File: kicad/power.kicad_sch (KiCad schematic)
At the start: 12 parts, among them J1 Bus_PCI_Express_x1, J2 Conn_01x02_Pin, J6 USB_C_Receptacle_USB2.0_16P

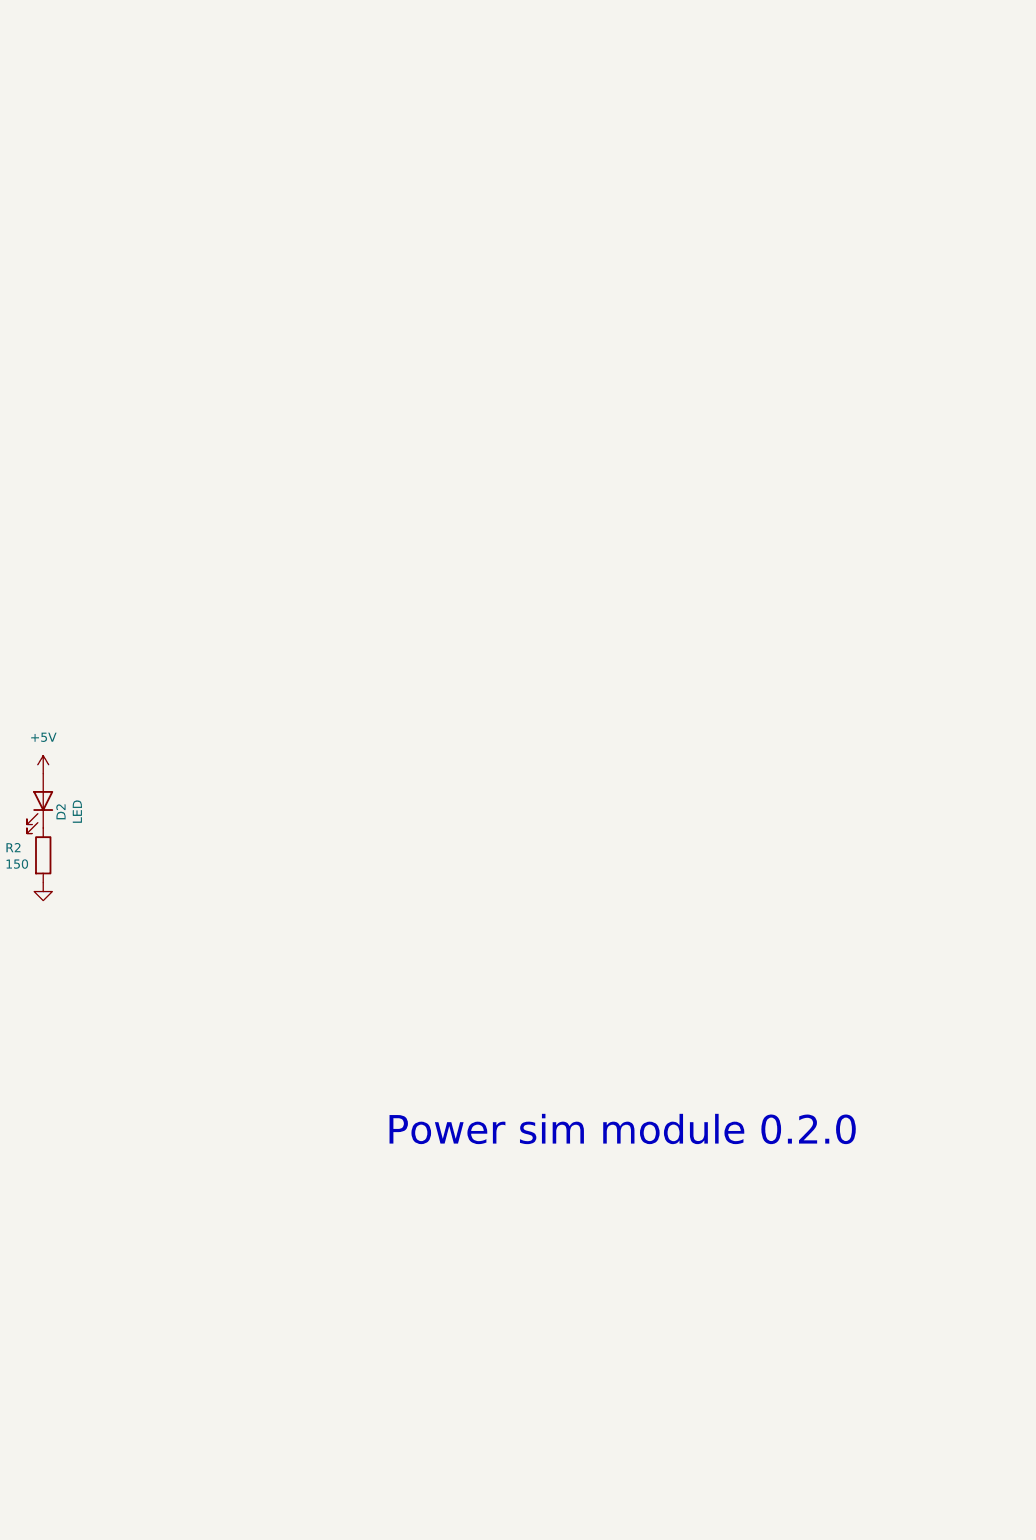
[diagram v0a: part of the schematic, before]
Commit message: feat: Add components for battery management, charging, and protection
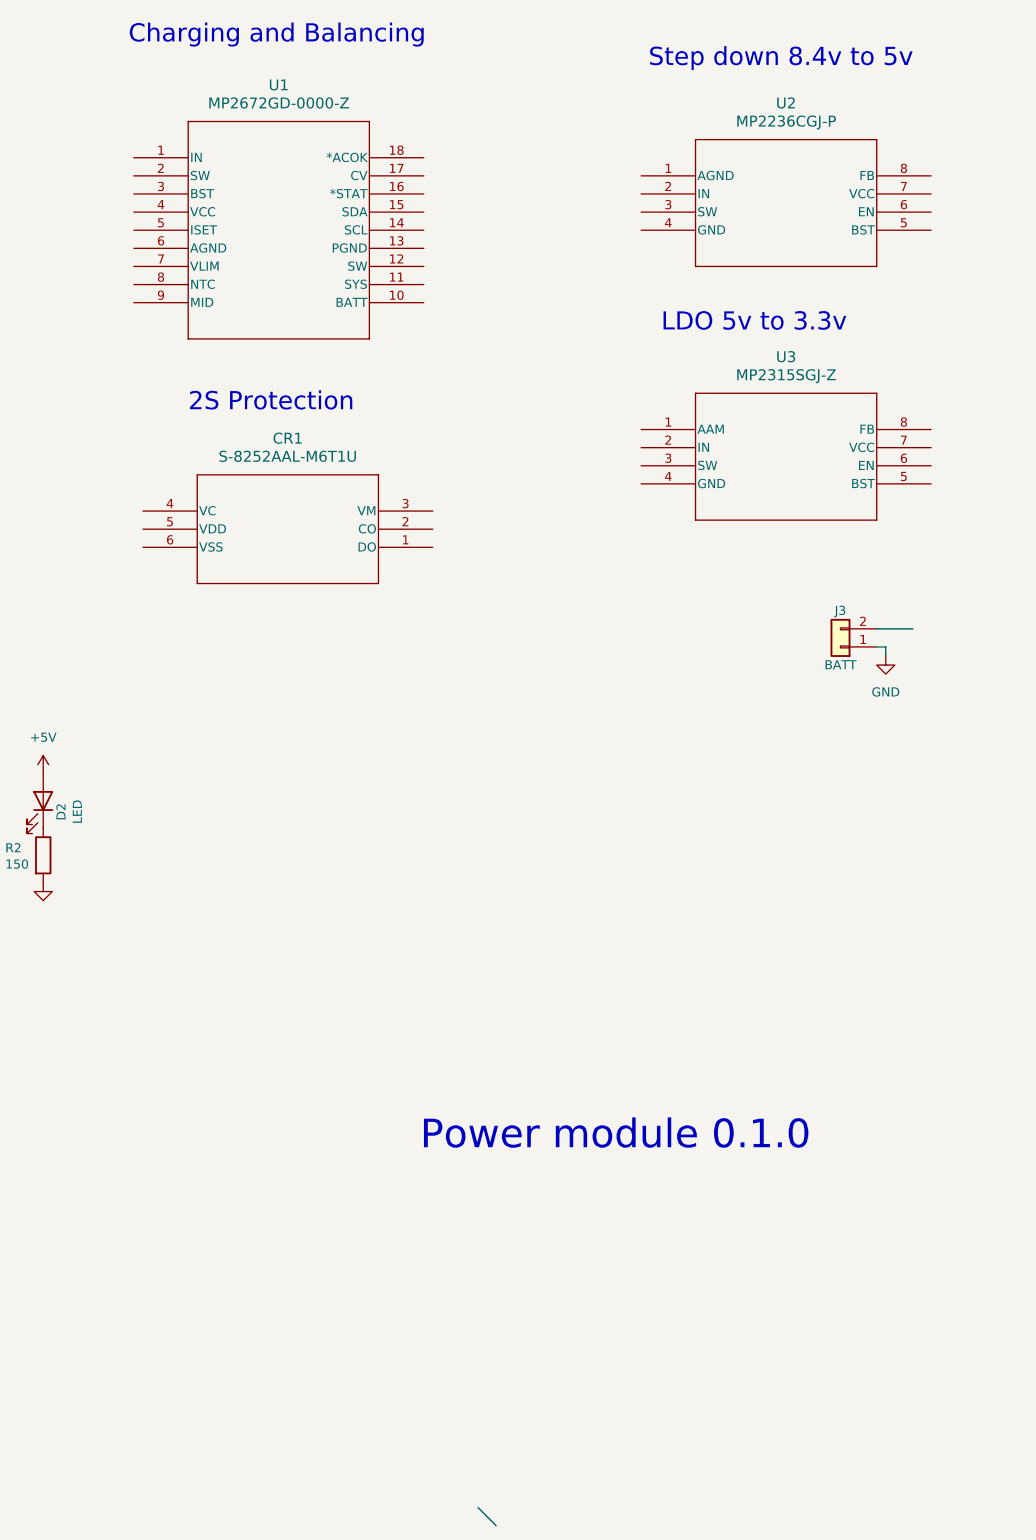
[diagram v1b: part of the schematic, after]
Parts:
- added CR1: S-8252AAL-M6T1U, SOT23-6L_STM, symbol powermodule:S-8252AAL-M6T1U
- added J3: BATT, Connector_AMASS:AMASS_XT30U-F_1x02_P5.0mm_Vertical, symbol Connector_Generic:Conn_01x02
- added U1: MP2672GD-0000-Z, POWERLIB:QFN-18_2MMx3MM_MP2672_MNP_MPS, symbol powermodule:MP2672GD-0000-Z
- added U2: MP2236CGJ-P, POWERLIB:TSOT23-8_MP2236C_MNP, symbol powermodule:MP2236CGJ-P
- added U3: MP2315SGJ-Z, TSOT23-8_MP2315S_MNP, symbol powermodule:MP2315SGJ-Z
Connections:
- net GND: now also J3.1 (Pin_1)
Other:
- note added: "2S Protection"
- note added: "Charging and Balancing"
- note added: "LDO 5v to 3.3v"
- note added: "Power module 0.1.0"
- note added: "Step down 8.4v to 5v"
- note removed: "Power sim module 0.2.0"

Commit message: feat: Update 2S protection
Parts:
- added C1, C2: 0.1u, Capacitor_SMD:C_0402_1005Metric, symbol Device:C
- added Q1, Q2: AO3400A, SOT-23-3_L2.9-W1.3-P1.90-LS2.4-BR, symbol powermodule:AO3400
- added R5: 2k, Resistor_SMD:R_0402_1005Metric, symbol Device:R
- added R6, R7: 470R, Resistor_SMD:R_0402_1005Metric, symbol Device:R
- R1, R2: value 150 -> 1k; footprint Resistor_SMD:R_0603_1608Metric -> Resistor_SMD:R_0402_1005Metric; JLC Link https://jlcpcb.com/partdetail/23535-0603WAF1500T5E/C22808 -> https://jlcpcb.com/partdetail/12256-0402WGF1001TCE/C11702; LCSC Part # C22808 -> C11702; info 150 ohm -> 1k ohm; price C$0.0013 -> C$0.0007
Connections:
- net at CR1.1 (DO): now also Q2.1 (G)
- net at CR1.2 (CO): now also Q1.3 (D), Q2.3 (D)
- net at CR1.3 (VM): now also R5.2
- net at CR1.4 (VC): now also C2.2, R7.2
- net at CR1.5 (VDD): now also C1.1, R6.2
- net B_GND: now reaches CR1.6 (VSS)
- net B_GND: now also C1.2, C2.1, Q2.2 (S)
- new net +4.2V: R7.1
- new net +8.4V: R6.1
- new net LOAD_GND: Q1.2 (S), R5.1
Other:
- moved on the sheet: CR1

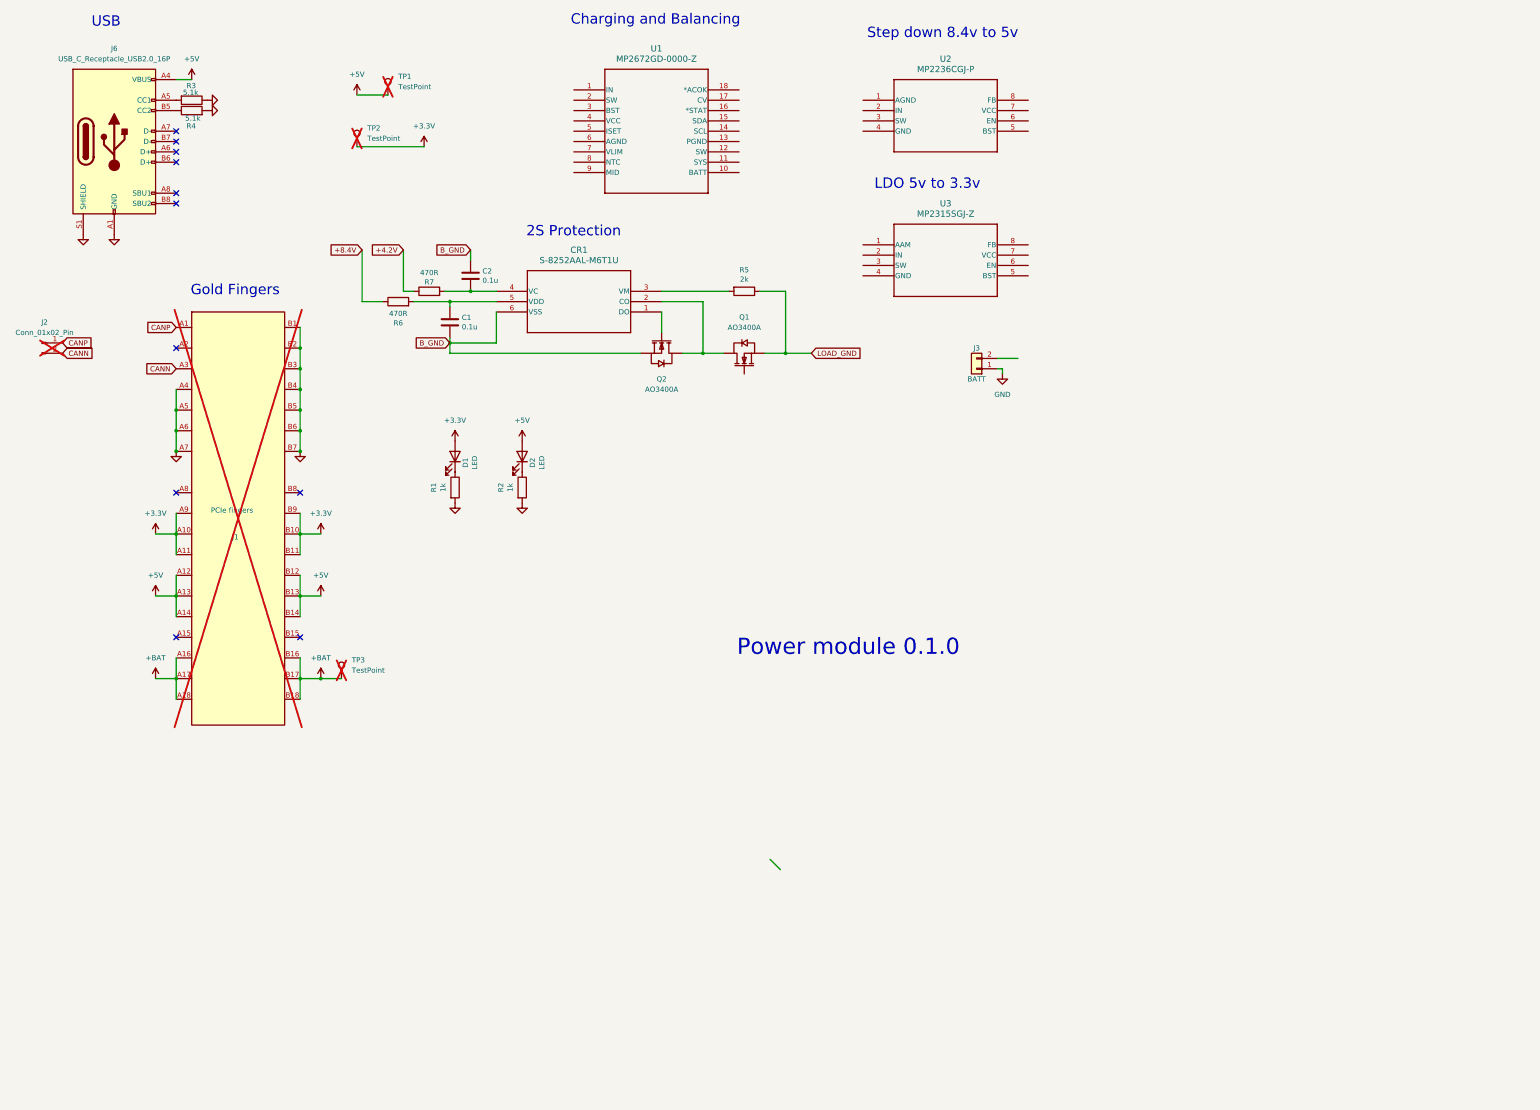
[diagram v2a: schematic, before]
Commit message: feat: Update 8.4V to 5V DC-DC converter
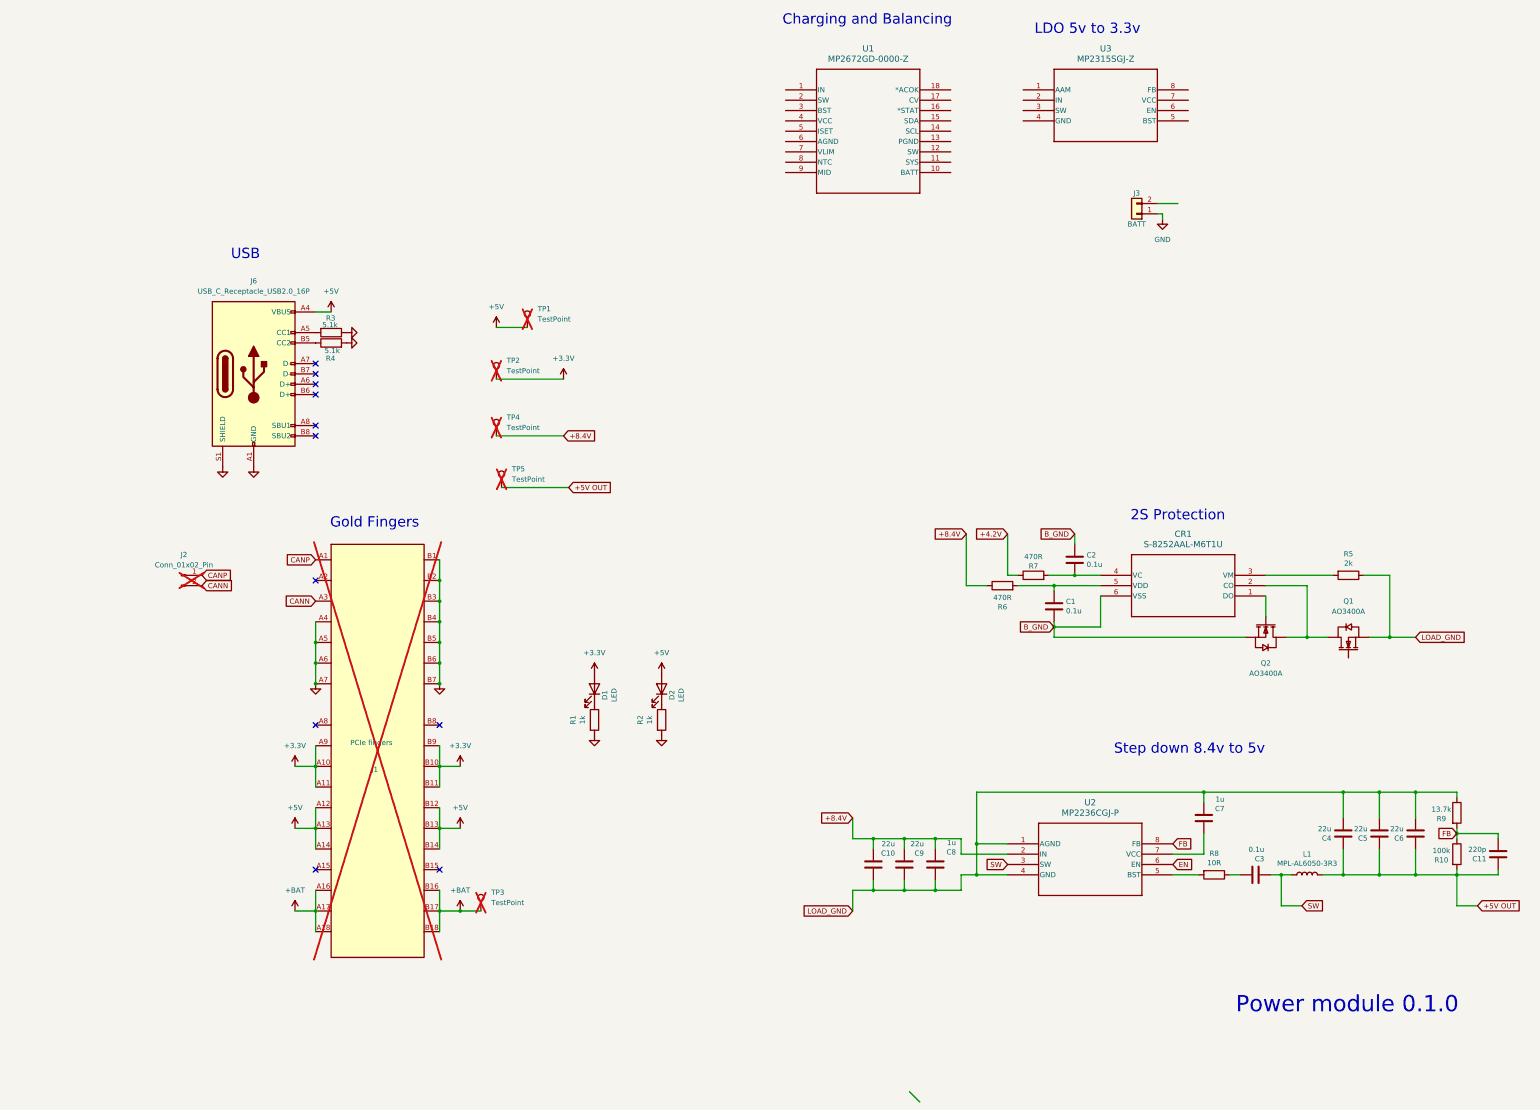
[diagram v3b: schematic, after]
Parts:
- added C10, C4, C5, C6, C9: 22u, Capacitor_SMD:C_0402_1005Metric, symbol Device:C
- added C11: 220p, Capacitor_SMD:C_0402_1005Metric, symbol Device:C
- added C3: 0.1u, Capacitor_SMD:C_0402_1005Metric, symbol Device:C
- added C7, C8: 1u, Capacitor_SMD:C_0402_1005Metric, symbol Device:C
- added L1: MPL-AL6050-3R3, POWERLIB:2-SMD, symbol Device:L
- added R10: 100k, Resistor_SMD:R_0402_1005Metric, symbol Device:R
- added R8: 10R, Resistor_SMD:R_0402_1005Metric, symbol Device:R
- added R9: 13.7k, Resistor_SMD:R_0402_1005Metric, symbol Device:R
- added TP4, TP5: TestPoint, Connector_PinHeader_2.54mm:PinHeader_1x01_P2.54mm_Vertical, symbol Connector:TestPoint
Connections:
- net +8.4V: now also U2.2 (IN), C10.2, C8.1, C9.2, TP4.1
- net LOAD_GND: now also U2.1 (AGND), U2.4 (GND), C10.1, C4.2, C5.2, C6.2, C7.1, C8.2, C9.1, R9.1
- net SW: now reaches U2.3 (SW)
- net SW: now also C3.2, L1.1
- net at U2.5 (BST): now also R8.2
- net EN: now reaches U2.6 (EN)
- net at U2.7 (VCC): now also C7.2
- net FB: now reaches U2.8 (FB)
- net FB: now also C11.2, R10.1, R9.2
- new net: C3.1, R8.1
- new net +5V OUT: C11.1, C4.1, C5.1, C6.1, L1.2, R10.2, TP5.1
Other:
- moved on the sheet: C1, C2, CR1, D1, D2, J1, J2, J3, J6, Q1, Q2, R1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

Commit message: feat: Update 8.4V to 3.3V DC-DC converter
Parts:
- removed U3: MP2315SGJ-Z, TSOT23-8_MP2315S_MNP, symbol powermodule:MP2315SGJ-Z
- added C12, C13, C17, C18, C19: 22u, Capacitor_SMD:C_0402_1005Metric, symbol Device:C
- added C14, C15: 1u, Capacitor_SMD:C_0402_1005Metric, symbol Device:C
- added C16: 0.1u, Capacitor_SMD:C_0402_1005Metric, symbol Device:C
- added C20: 220p, Capacitor_SMD:C_0402_1005Metric, symbol Device:C
- added L2: MPL-AL6050-2R2, POWERLIB:2-SMD, symbol Device:L
- added R11: 10R, Resistor_SMD:R_0402_1005Metric, symbol Device:R
- added R12: 22.1k, Resistor_SMD:R_0402_1005Metric, symbol Device:R
- added R13: 100k, Resistor_SMD:R_0402_1005Metric, symbol Device:R
- added U3: MP2236CGJ-P, POWERLIB:TSOT23-8_MP2236C_MNP, symbol powermodule:MP2236CGJ-P
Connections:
- net EN is gone; now on net +8.4V: U2.6 (EN)
- net +8.4V: now also C12.2, C13.2, C14.1, U3.2 (IN), U3.6 (EN)
- net LOAD_GND: now also C12.1, C13.1, C14.2, C15.1, C17.2, C18.2, C19.2, R12.1, U3.1 (AGND), U3.4 (GND)
- net FB renamed FB1
- net SW renamed SW1
- new net: C15.2, U3.7 (VCC)
- new net: C16.1, R11.1
- new net: R11.2, U3.5 (BST)
- new net +3.3V OUT: C17.1, C18.1, C19.1, C20.1, L2.2, R13.2
- new net FB2: C20.2, R12.2, R13.1, U3.8 (FB)
- new net SW2: C16.2, L2.1, U3.3 (SW)
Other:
- moved on the sheet: C1, C10, C11, C2, C3, C4, C5, C6, C7, C8, C9, CR1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

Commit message: feat: add charging
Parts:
- removed J3: BATT, Connector_AMASS:AMASS_XT30U-F_1x02_P5.0mm_Vertical, symbol Connector_Generic:Conn_01x02
- removed TP1: TestPoint, Connector_PinHeader_2.54mm:PinHeader_1x01_P2.54mm_Vertical, symbol Connector:TestPoint
- added C21, C24: 10u, Capacitor_SMD:C_0402_1005Metric, symbol Device:C
- added C22, C25: 22u, Capacitor_SMD:C_0402_1005Metric, symbol Device:C
- added C23: 1u, Capacitor_SMD:C_0402_1005Metric, symbol Device:C
- added C26: 100n, Capacitor_SMD:C_0402_1005Metric, symbol Device:C
- added D3, D4: LED, symbol Device:LED
- added L3: 1.5uH, IND-SMD_L7.0-W6.6, symbol powermodule:MWSA0605S-1R5MT
- added R14: 5.5k, Resistor_SMD:R_0402_1005Metric, symbol Device:R
- added R15, R24: 100R, Resistor_SMD:R_0402_1005Metric, symbol Device:R
- added R16: 30k, Resistor_SMD:R_0402_1005Metric, symbol Device:R
- added R17, R23: 60R, Resistor_SMD:R_0402_1005Metric, symbol Device:R
- added R18: 8k, Resistor_SMD:R_0402_1005Metric, symbol Device:R
- added R19: 12.6k, Resistor_SMD:R_0402_1005Metric, symbol Device:R
- added R20: 3.6k, Resistor_SMD:R_0402_1005Metric, symbol Device:R
- added R21: 2k, Resistor_SMD:R_0402_1005Metric, symbol Device:R
- added R22: NTCG103JF103FT1, POWERLIB:NTC_R0402, symbol powermodule:NTCG103JF103FT1
- added TP6: TestPoint, Connector_PinHeader_2.54mm:PinHeader_1x01_P2.54mm_Vertical, symbol Connector:TestPoint
- added U4: MR30-M, POWERLIB:CONN-TH_MR30-M, symbol powermodule:MR30
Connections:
- net +3.3V: no longer TP2.1
- net +3.3V OUT: now also TP2.1
- net +4.2V: now also R17.2, R23.2, TP6.1, U4.2
- net +5V: no longer J6.A4 (VBUS), J6.A9 (VBUS), J6.B4 (VBUS), J6.B9 (VBUS)
- net +8.4V: now also U1.10 (BATT), C25.1, U4.1
- net B_GND: now also U4.3
- net GND: no longer J6.A1 (GND), J6.A12 (GND), J6.B1 (GND), J6.B12 (GND), J6.S1 (SHIELD), R3.1, R4.2
- net LOAD_GND: now also J6.A1 (GND), J6.A12 (GND), J6.B1 (GND), J6.B12 (GND), J6.S1 (SHIELD), R3.1, R4.2, U1.13 (PGND), U1.6 (AGND), C21.2, C22.1, C23.2, C24.2, C25.2, R16.2, R18.2, R21.1, R22.1
- net VIN: now reaches U1.1 (IN)
- net VIN: now also J6.A4 (VBUS), J6.A9 (VBUS), J6.B4 (VBUS), J6.B9 (VBUS), C21.1, C24.1, L3.1, R14.2
- net at U1.11 (SYS): now also C22.2
- net SCL: now reaches U1.14 (SCL)
- net SDA: now reaches U1.15 (SDA)
- net at U1.16 (*STAT): now also D4.1 (K)
- net at U1.17 (CV): now also R16.1
- net at U1.18 (*ACOK): now also D3.1 (K)
- net at U1.2 (SW): now also C26.1, L3.2
- net at U1.3 (BST): now also C26.2
- net VCC: now reaches U1.4 (VCC)
- net VCC: now also C23.1, R15.1, R19.1, R24.1
- net at U1.5 (ISET): now also R18.1
- net VLIM: now reaches U1.7 (VLIM)
- net VLIM: now also R14.1, R21.2
- net at U1.8 (NTC): now also R19.2, R20.2
- net at U1.9 (MID): now also R17.1, R23.1
- new net: R20.1, R22.2
- new net: D4.2 (A), R24.2
- new net: D3.2 (A), R15.2
- no-connect marks 11 -> 12
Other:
- note added: "Step down 5v to 3.3v"
- note removed: "LDO 5v to 3.3v"
- moved on the sheet: C10, C11, C12, C13, C14, C15, C16, C17, C18, C19, C20, C3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
